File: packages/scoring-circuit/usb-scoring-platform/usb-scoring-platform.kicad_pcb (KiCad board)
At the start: 4 copper layers, 160 x 100 mm, 153 parts, among them J1 GCT USB4105-GF-A, J10 5520250-2, J2 STM SWD 3.3V, J3 LEFT WEAPON A B C, J4 RIGHT WEAPON A B C, J5 PISTE - NOT protective earth, J6 ESP 3.3V UART recovery, J7 TST-108-02-G-D - HUB75, J8 645004114822 - panel 5V, J9 5520250-2, Q1 BSS138-7-F, Q2 BSS138-7-F, Q3 BSS138-7-F, SW1 STM RESET, SW2 ESP RESET, SW3 ESP BOOT, U1 STM32G474RET6, U10 SN74AXC1T45DCKR, U11 SN74AXC1T45DCKR, U12 WIZ850io, U13 TSOP38438, U14 SN74AHCT245PWR, U15 SN74AHCT245PWR, U16 4N32M, U17 4N32M, U18 LTM2884IY#PBF, U2 ESP32-S3-WROOM-1-N8R8, U3 USBLC6-2SC6, U4 AP2112K-3.3TRG1, U5 Adafruit 5807 - set 20V, U6 D36V50F5, U7 AP63203WU-7, U8 74LVC125APW, U9 74LVC125APW, Y1 ABM3B-8.000MHZ-B2-T

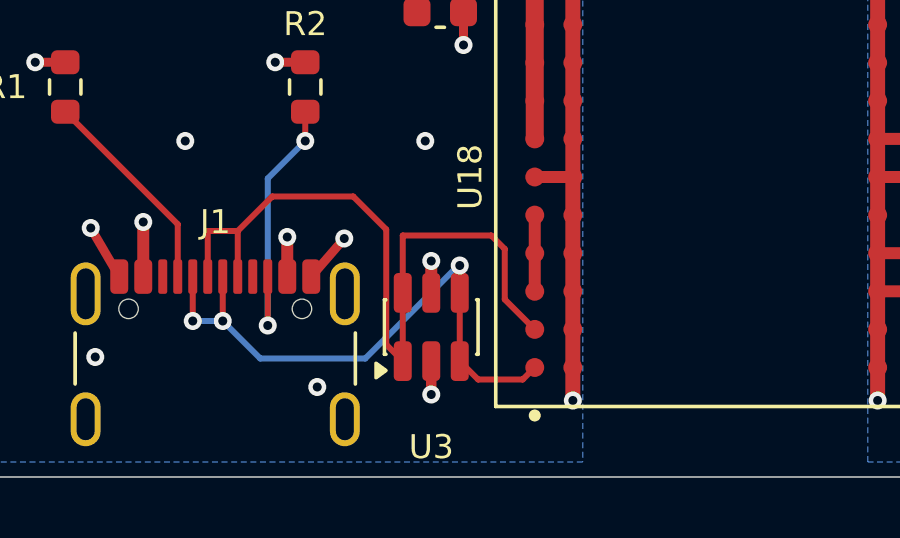
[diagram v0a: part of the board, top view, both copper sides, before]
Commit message: feat(scoring-circuit): decouple USB data protection from VBUS
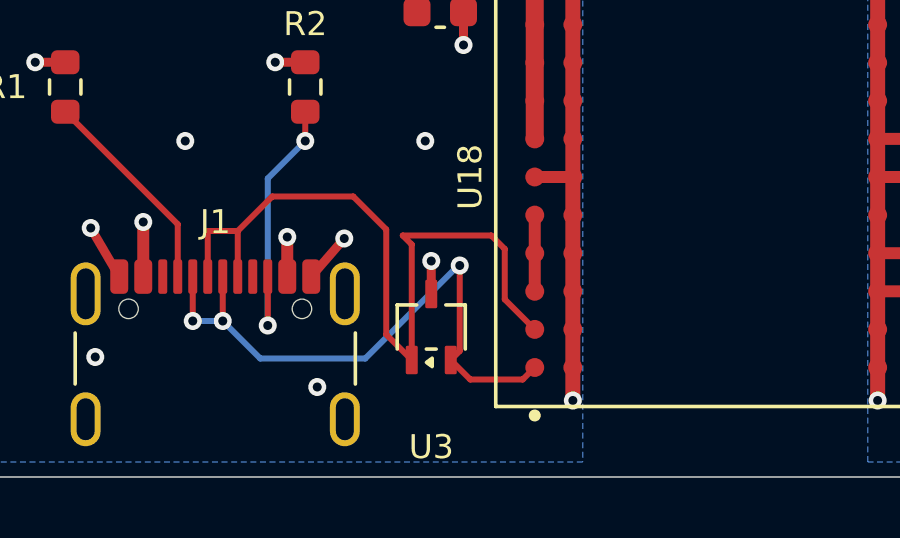
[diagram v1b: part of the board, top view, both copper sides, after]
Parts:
- C1: value 1uF 10V -> 1uF 50V
- U3: value USBLC6-2SC6 -> TPD2E2U06DCKR; footprint Package_TO_SOT_SMD:SOT-23-6 -> ScoringPlatform:TPD2E2U06DCKR
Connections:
- U3 pad 2: USB_GND -> USB_HOST_DM
- U3 pad 3: USB_HOST_DM -> USB_GND
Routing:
- net USB_VBUS: track 55.9 -> 41.8 mm, vias 4 -> 3
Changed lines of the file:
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@@
 			)
 		)
-		(property "Value" "1uF 10V"
+		(property "Value" "1uF 50V"
 			(at 0 1.43 0)
 			(layer "F.Fab")
@@
 		)
 	)
-	(footprint "Package_TO_SOT_SMD:SOT-23-6"
+	(footprint "ScoringPlatform:TPD2E2U06DCKR"
 		(layer "F.Cu")
 		(at 72.2 145 90)
-		(descr "SOT, 6 Pin (JEDEC MO-178 Var AB https://www.jedec.org/document_search?search_api_views_fulltext=MO-178)")
-		(tags "SOT TO_SOT_SMD")
+		(descr "TI TPD2E2U06DCKR, DCK0003A: SC70-3, 0.95 x 0.4 mm lands, 2.2 mm row span, 1.3 mm pin 1/2 pitch. Datasheet SLLSEG9C; land drawing 4220745/F.")
+		(tags "USB ESD TPD2E2U06 DCK SC70")
 		(property "Reference" "U3"
 			(at -4 0 0)
@@
 			)
 		)
-		(property "Value" "USBLC6-2SC6"
-			(at 0 2.4 90)
+		(property "Value" "TPD2E2U06DCKR"
+			(at 0 1.8 90)
 			(layer "F.Fab")
 			(hide yes)
@@
 			)
 		)
-		(property "Datasheet" ""
+		(property "Datasheet" "https://www.ti.com/lit/ds/symlink/tpd2e2u06.pdf"
 			(at 0 0 90)
 			(layer "F.Fab")
@@
 		(duplicate_pad_numbers_are_jumpers no)
 		(fp_line
-			(start 0.91 -1.56)
-			(end 0.91 -1.51)
+			(start 0.735 -1.135)
+			(end 0.735 -0.485)
 			(stroke
 				(width 0.12)
@@
 		)
 		(fp_line
-			(start -0.91 -1.56)
-			(end 0.91 -1.56)
+			(start -0.735 -1.135)
+			(end 0.735 -1.135)
 			(stroke
 				(width 0.12)
@@
 		)
 		(fp_line
-			(start -0.91 -1.51)
-			(end -0.91 -1.56)
+			(start -0.735 0.165)
+			(end -0.735 -0.165)
 			(stroke
 				(width 0.12)
@@
 		)
 		(fp_line
-			(start 0.91 1.51)
-			(end 0.91 1.56)
+			(start 0.735 0.485)
+			(end 0.735 1.135)
 			(stroke
 				(width 0.12)
@@
 		)
 		(fp_line
-			(start 0.91 1.56)
-			(end -0.91 1.56)
+			(start 0.735 1.135)
+			(end -0.735 1.135)
 			(stroke
 				(width 0.12)
@@
 			(layer "F.SilkS")
 		)
-		(fp_line
-			(start -0.91 1.56)
-			(end -0.91 1.51)
+		(fp_poly
+			(pts
+				(xy -1.18 -0.16) (xy -1.04 0.03) (xy -1.32 0.03)
+			)
 			(stroke
 				(width 0.12)
 				(type solid)
 			)
+			(fill yes)
 			(layer "F.SilkS")
 		)
-		(fp_poly
-			(pts
-				(xy -1.45 -1.51) (xy -1.69 -1.84) (xy -1.21 -1.84)
+		(fp_line
+			(start 0.92131 -1.1)
+			(end 0.92131 -0.45)
+			(stroke
+				(width 0.05)
+				(type solid)
 			)
+			(layer "F.CrtYd")
+		)
+		(fp_line
+			(start -0.92131 -1.1)
+			(end 0.92131 -1.1)
 			(stroke
-				(width 0.12)
+				(width 0.05)
 				(type solid)
 			)
-			(fill yes)
-			(layer "F.SilkS")
+			(layer "F.CrtYd")
 		)
 		(fp_line
-			(start 1.05 -1.7)
-			(end 1.05 -1.5)
+			(start -0.92131 -0.98)
+			(end -0.92131 -1.1)
 			(stroke
 				(width 0.05)
@@
 		)
 		(fp_line
-			(start -1.05 -1.7)
-			(end 1.05 -1.7)
+			(start -1.83 -0.98)
+			(end -0.92131 -0.98)
 			(stroke
 				(width 0.05)
@@
 		)
 		(fp_line
-			(start 2.05 -1.5)
-			(end 2.05 1.5)
+			(start 1.83 -0.45)
+			(end 1.83 0.45)
 			(stroke
 				(width 0.05)
@@
 		)
 		(fp_line
-			(start 1.05 -1.5)
-			(end 2.05 -1.5)
+			(start 0.92131 -0.45)
+			(end 1.83 -0.45)
 			(stroke
 				(width 0.05)
@@
 		)
 		(fp_line
-			(start -1.05 -1.5)
-			(end -1.05 -1.7)
+			(start -0.92131 -0.32)
+			(end -1.83 -0.32)
 			(stroke
 				(width 0.05)
@@
 		)
 		(fp_line
-			(start -2.05 -1.5)
-			(end -1.05 -1.5)
+			(start -1.83 -0.32)
+			(end -1.83 -0.98)
 			(stroke
 				(width 0.05)
@@
 		)
 		(fp_line
-			(start 2.05 1.5)
-			(end 1.05 1.5)
+			(start -0.92131 0.32)
+			(end -0.92131 -0.32)
 			(stroke
 				(width 0.05)
@@
 		)
 		(fp_line
-			(start 1.05 1.5)
-			(end 1.05 1.7)
+			(start -1.83 0.32)
+			(end -0.92131 0.32)
 			(stroke
 				(width 0.05)
@@
 		)
 		(fp_line
-			(start -1.05 1.5)
-			(end -2.05 1.5)
+			(start 1.83 0.45)
+			(end 0.92131 0.45)
 			(stroke
 				(width 0.05)
@@
 		)
 		(fp_line
-			(start -2.05 1.5)
-			(end -2.05 -1.5)
+			(start 0.92131 0.45)
+			(end 0.92131 1.1)
 			(stroke
 				(width 0.05)
@@
 		)
 		(fp_line
-			(start 1.05 1.7)
-			(end -1.05 1.7)
+			(start -0.92131 0.98)
+			(end -1.83 0.98)
 			(stroke
 				(width 0.05)
@@
 		)
 		(fp_line
-			(start -1.05 1.7)
-			(end -1.05 1.5)
+			(start -1.83 0.98)
+			(end -1.83 0.32)
+			(stroke
+				(width 0.05)
+				(type solid)
+			)
+			(layer "F.CrtYd")
+		)
+		(fp_line
+			(start 0.92131 1.1)
+			(end -0.92131 1.1)
+			(stroke
+				(width 0.05)
+				(type solid)
+			)
+			(layer "F.CrtYd")
+		)
+		(fp_line
+			(start -0.92131 1.1)
+			(end -0.92131 0.98)
 			(stroke
 				(width 0.05)
@@
 		(fp_poly
 			(pts
-				(xy -0.4 -1.45) (xy 0.8 -1.45) (xy 0.8 1.45) (xy -0.8 1.45) (xy -0.8 -1.05)
+				(xy -0.3125 -1) (xy 0.625 -1) (xy 0.625 1) (xy -0.625 1) (xy -0.625 -0.6875)
 			)
 			(stroke
@@
 			(effects
 				(font
-					(size 0.72 0.72)
-					(thickness 0.11)
+					(size 0.5 0.5)
+					(thickness 0.08)
 				)
 			)
 		)
 		(pad "1" smd roundrect
-			(at -1.1375 -0.95 90)
-			(size 1.325 0.6)
+			(at -1.1 -0.65 90)
+			(size 0.95 0.4)
 			(layers "F.Cu" "F.Mask" "F.Paste")
-			(roundrect_rratio 0.25)
+			(roundrect_rratio 0.125)
 			(net "USB_HOST_DP")
 		)
 		(pad "2" smd roundrect
-			(at -1.1375 0 90)
-			(size 1.325 0.6)
-			(layers "F.Cu" "F.Mask" "F.Paste")
-			(roundrect_rratio 0.25)
-			(net "USB_GND")
-		)
-		(pad "3" smd roundrect
-			(at -1.1375 0.95 90)
-			(size 1.325 0.6)
-			(layers "F.Cu" "F.Mask" "F.Paste")
-			(roundrect_rratio 0.25)
-			(net "USB_HOST_DM")
-		)
-		(pad "4" smd roundrect
-			(at 1.1375 0.95 90)
-			(size 1.325 0.6)
+			(at -1.1 0.65 90)
+			(size 0.95 0.4)
 			(layers "F.Cu" "F.Mask" "F.Paste")
-			(roundrect_rratio 0.25)
+			(roundrect_rratio 0.125)
 			(net "USB_HOST_DM")
 		)
-		(pad "5" smd roundrect
-			(at 1.1375 0 90)
-			(size 1.325 0.6)
-			(layers "F.Cu" "F.Mask" "F.Paste")
-			(roundrect_rratio 0.25)
-			(net "USB_VBUS")
-		)
-		(pad "6" smd roundrect
-			(at 1.1375 -0.95 90)
-			(size 1.325 0.6)
+		(pad "3" smd roundrect
+			(at 1.1 0 90)
+			(size 0.95 0.4)
 			(layers "F.Cu" "F.Mask" "F.Paste")
-			(roundrect_rratio 0.25)
-			(net "USB_HOST_DP")
+			(roundrect_rratio 0.125)
+			(net "USB_GND")
 		)
 		(embedded_fonts no)
-		(model "${KICAD10_3DMODEL_DIR}/Package_TO_SOT_SMD.3dshapes/SOT-23-6.step"
+		(model "${KICAD10_3DMODEL_DIR}/Package_TO_SOT_SMD.3dshapes/SOT-323_SC-70.step"
 			(offset
 				(xyz 0 0 0)
@@
 		(net "USB_VBUS")
 	)
-	(segment
-		(start 72.2 143.8625)
-		(end 72.2 142.8)
-		(width 0.4)
-		(layer "F.Cu")
-		(net "USB_VBUS")
-	)
-	(via
-		(at 72.2 142.8)
-		(size 0.6)
-		(drill 0.3)
-		(layers "F.Cu" "B.Cu")
-		(net "USB_VBUS")
-	)
 	(via
 		(at 71.725 133.4)
@@
 	)
 	(segment
-		(start 72.2 142.8)
-		(end 74.4 140.6)
-		(width 0.4)
-		(layer "In2.Cu")
-		(net "USB_VBUS")
-	)
-	(segment
 		(start 62.6 141.5)
 		(end 62.6 135.5)
@@
 	)
 	(segment
-		(start 74.4 140.6)
-		(end 74.4 133.4)
-		(width 0.4)
-		(layer "In2.Cu")
-		(net "USB_VBUS")
-	)
-	(segment
 		(start 62.6 135.5)
 		(end 64.7 133.4)
@@
 	)
 	(segment
-		(start 74.4 133.4)
-		(end 71.725 133.4)
-		(width 0.4)
-		(layer "In2.Cu")
-		(net "USB_VBUS")
-	)
-	(segment
-		(start 72.2 146.1375)
-		(end 72.2 147.25)
-		(width 0.35)
-		(layer "F.Cu")
-		(net "USB_GND")
-	)
-	(segment
 		(start 73.275 134.5)
 		(end 73.275 135.6)
@@
 	)
 	(segment
+		(start 72.2 143.9)
+		(end 72.2 142.8)
+		(width 0.3)
+		(layer "F.Cu")
+		(net "USB_GND")
+	)
+	(segment
 		(start 60 136.175)
 		(end 59 136.175)
@@
 	)
 	(via
-		(at 59 136.175)
+		(at 72.2 142.8)
 		(size 0.6)
 		(drill 0.3)
@@
 	)
 	(via
-		(at 72.2 147.25)
+		(at 59 136.175)
 		(size 0.6)
 		(drill 0.3)
@@
 	)
 	(segment
-		(start 70.7 145.5875)
-		(end 71.25 146.1375)
+		(start 71.55 142.25)
+		(end 71.25 141.95)
+		(width 0.2)
+		(layer "F.Cu")
+		(net "USB_HOST_DP")
+	)
+	(segment
+		(start 70.7 145.25)
+		(end 71.55 146.1)
 		(width 0.2)
 		(layer "F.Cu")
@@
 	(segment
 		(start 70.7 141.75)
-		(end 70.7 145.5875)
+		(end 70.7 145.25)
 		(width 0.2)
 		(layer "F.Cu")
@@
 	)
 	(segment
-		(start 71.25 146.1375)
-		(end 71.25 141.95)
+		(start 71.55 146.1)
+		(end 71.55 142.25)
 		(width 0.2)
 		(layer "F.Cu")
@@
 	)
 	(segment
-		(start 73.7625 146.75)
+		(start 73.5 146.75)
 		(end 75.25 146.75)
 		(width 0.2)
@@
 	(segment
 		(start 73.15 142.95)
-		(end 73.15 146.1375)
+		(end 73.15 145.8)
+		(width 0.2)
+		(layer "F.Cu")
+		(net "USB_HOST_DM")
+	)
+	(segment
+		(start 73.15 145.8)
+		(end 72.85 146.1)
 		(width 0.2)
 		(layer "F.Cu")
@@
 	)
 	(segment
-		(start 73.15 146.1375)
-		(end 73.7625 146.75)
+		(start 72.85 146.1)
+		(end 73.5 146.75)
 		(width 0.2)
 		(layer "F.Cu")

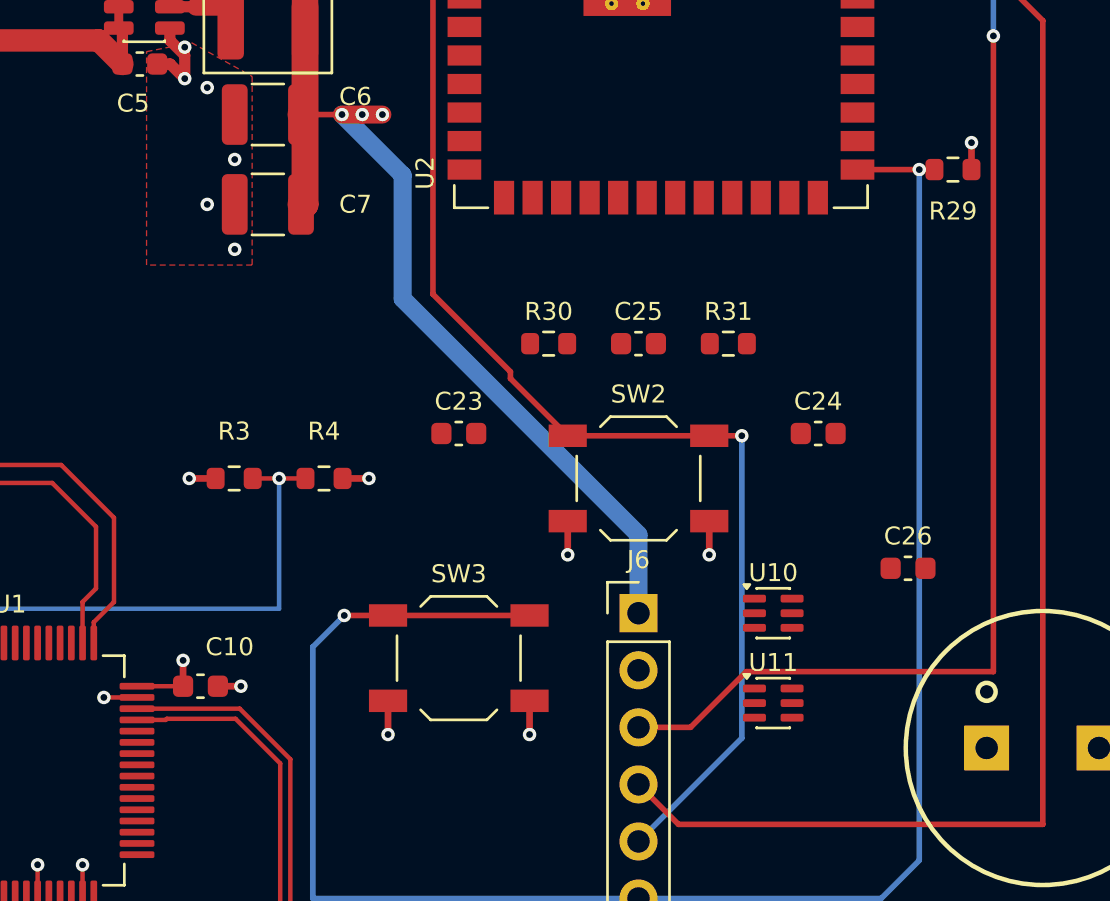
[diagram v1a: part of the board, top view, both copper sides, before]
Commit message: feat(scoring-circuit): route reset-safe processor UART link
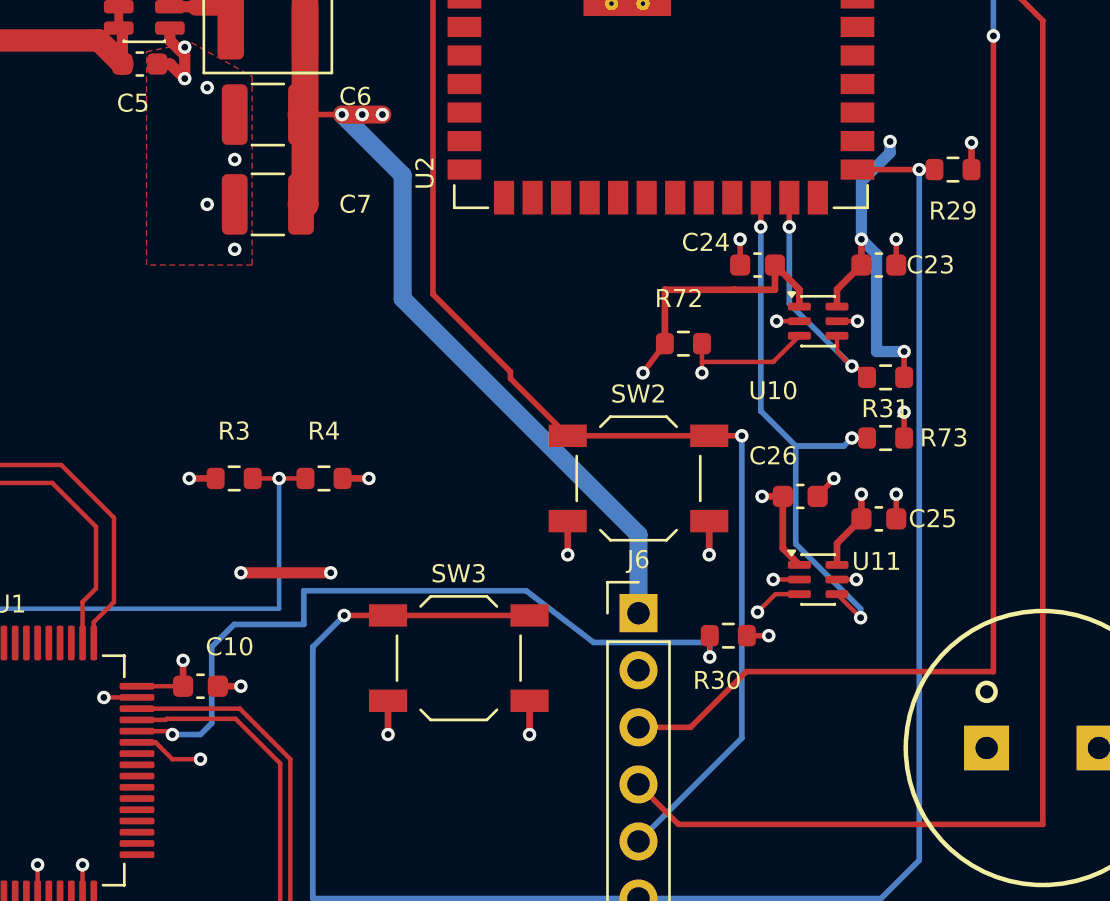
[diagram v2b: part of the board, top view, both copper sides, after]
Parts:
- added R72: 10k 1%, Resistor_SMD:R_0603_1608Metric, F.Cu at (147.0, 87.0)
- added R73: 10k 1%, Resistor_SMD:R_0603_1608Metric, F.Cu at (156.0, 91.2)
- moved C23 20.1 mm to (155.7, 83.5)
- moved R30 15.3 mm to (149.0, 100.0), turned to 180 degrees
- moved C25 13.2 mm to (155.7, 94.8)
- moved U10 13.2 mm to (153.0, 86.0)
- moved C24 7.97 mm to (150.3, 83.5), turned to 180 degrees
- moved R31 7.16 mm to (156.0, 88.5), turned to 180 degrees
- moved U11 5.85 mm to (153.0, 97.5)
- moved C26 5.77 mm to (152.2, 93.8)
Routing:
- net STM_TX: track 0.00 -> 48.2 mm, vias 0 -> 2
- net STM_RX: track 0.00 -> 38.6 mm, vias 0 -> 3
- net APP_3V3: track 63.6 -> 93.8 mm, vias 7 -> 12
- net CORE_3V3: track 60.3 -> 86.3 mm, vias 12 -> 18
- net ESP_TX: track 0.00 -> 25.4 mm, vias 0 -> 3
- net ESP_RX: track 0.00 -> 11.2 mm, vias 0 -> 2
- net GND: track 75.2 -> 82.7 mm, vias 51 -> 58

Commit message: feat(scoring-circuit): route filtered IR receiver interface
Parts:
- moved C30 50.7 mm to (203.2, 108.0)
- moved R32 43.4 mm to (199.0, 108.0)
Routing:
- net IR_RX: track 0.00 -> 86.5 mm, vias 0 -> 1
- net APP_3V3: track 93.8 -> 154.6 mm, vias 12 -> 13
- net IR_3V3: track 0.00 -> 10.1 mm
- net GND: track 82.7 -> 92.0 mm, vias 58 -> 59

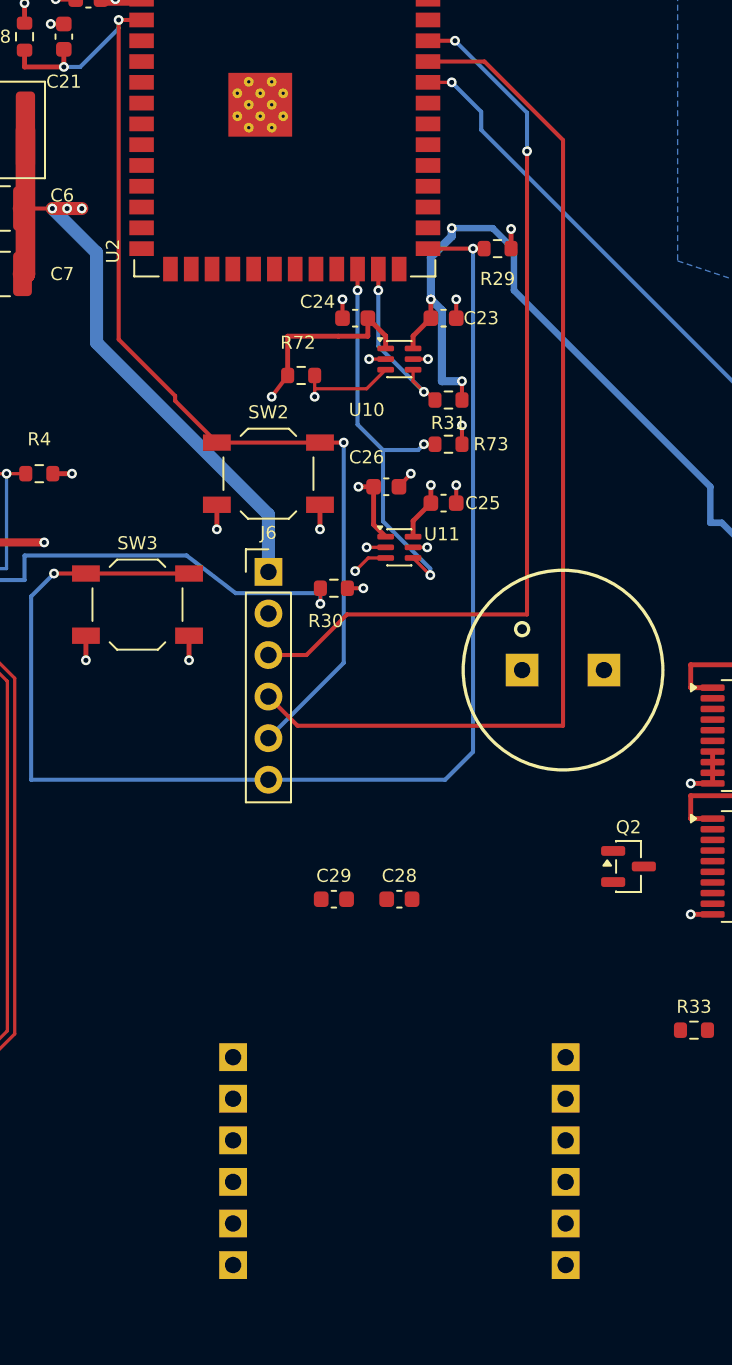
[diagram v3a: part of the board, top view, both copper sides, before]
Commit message: feat(scoring-circuit): route WIZ850io power and SPI interface
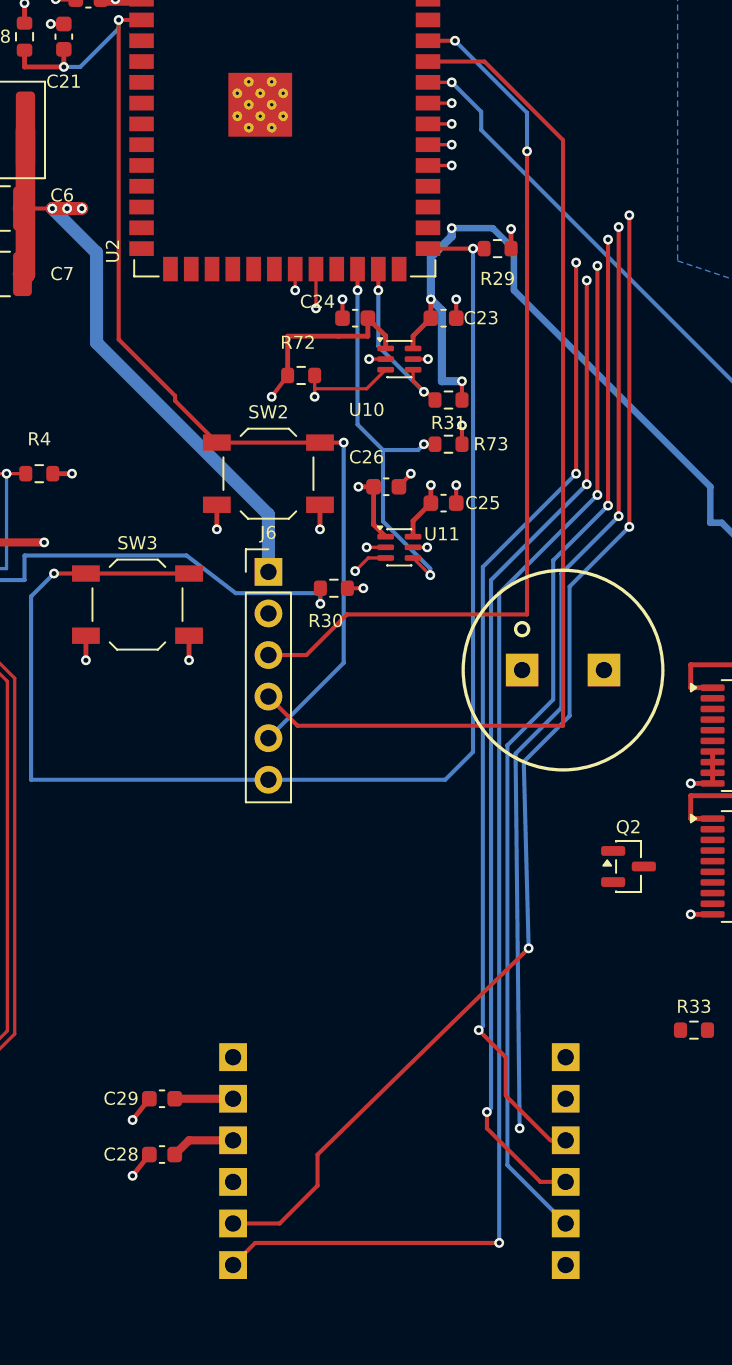
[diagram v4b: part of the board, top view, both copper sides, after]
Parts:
- moved C28 21.3 mm to (138.5, 134.6), turned to 180 degrees
- moved C29 16.1 mm to (138.5, 131.2), turned to 180 degrees
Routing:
- net ETH_MISO: track 0.00 -> 92.0 mm, vias 0 -> 4
- net ETH_RESET_N: track 0.00 -> 88.5 mm, vias 0 -> 4
- net ETH_IRQ_N: track 0.00 -> 83.6 mm, vias 0 -> 4
- net ETH_SCLK: track 0.00 -> 80.4 mm, vias 0 -> 4
- net ETH_MOSI: track 0.00 -> 77.9 mm, vias 0 -> 4
- net ETH_CS_N: track 0.00 -> 77.4 mm, vias 0 -> 3
- net APP_3V3: track 154.6 -> 215.3 mm
- net GND: track 92.0 -> 95.3 mm, vias 59 -> 61
